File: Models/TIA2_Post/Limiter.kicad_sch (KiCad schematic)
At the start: 18 parts, among them J1 Conn_01x02_Pin, J2 Conn_01x02_Pin, J3 Conn_01x02_Pin, J4 Conn_01x02_Pin, Q1 Q_PNP, Q2 Q_NPN

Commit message: Save progress
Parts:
- removed J3, J4: Conn_01x02_Pin, symbol Connector:Conn_01x02_Pin
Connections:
- net Output is gone; now on net PostVoltage: R14.1, R15.1
- net PostVoltage: now also R8.1
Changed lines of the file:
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@@
+	(wire
+		(pts
+			(xy 207.01 105.41) (xy 205.74 105.41)
+		)
+		(stroke
+			(width 0)
+			(type default)
+		)
+	)
+	(wire
+		(pts
+			(xy 213.36 115.57) (xy 213.36 121.92)
+		)
+		(stroke
+			(width 0)
+			(type default)
+		)
+	)
+	(wire
+		(pts
+			(xy 96.52 96.52) (xy 111.76 96.52)
+		)
+		(stroke
+			(width 0)
+			(type default)
+		)
+	)
+	(wire
+		(pts
+			(xy 205.74 115.57) (xy 213.36 115.57)
+		)
+		(stroke
+			(width 0)
+			(type default)
+		)
+	)
+	(wire
+		(pts
+			(xy 86.36 88.9) (xy 86.36 96.52)
+		)
+		(stroke
+			(width 0)
+			(type default)
+		)
+	)
+	(wire
+		(pts
+			(xy 40.64 96.52) (xy 45.72 96.52)
+		)
+		(stroke
+			(width 0)
+			(type default)
+		)
+	)
+	(wire
+		(pts
+			(xy 172.72 142.24) (xy 177.8 142.24)
+		)
+		(stroke
+			(width 0)
+			(type default)
+		)
+	)
+	(wire
+		(pts
+			(xy 190.5 83.82) (xy 190.5 96.52)
+		)
+		(stroke
+			(width 0)
+			(type default)
+		)
+	)
+	(wire
+		(pts
+			(xy 213.36 88.9) (xy 213.36 90.17)
+		)
+		(stroke
+			(width 0)
+			(type default)
+		)
+	)
+	(wire
+		(pts
+			(xy 190.5 50.8) (xy 190.5 58.42)
+		)
+		(stroke
+			(width 0)
+			(type default)
+		)
+	)
+	(wire
+		(pts
+			(xy 213.36 114.3) (xy 213.36 115.57)
+		)
+		(stroke
+			(width 0)
+			(type default)
+		)
+	)
 	(wire
 		(pts
@@
 	(wire
 		(pts
-			(xy 207.01 105.41) (xy 205.74 105.41)
-		)
-		(stroke
-			(width 0)
-			(type default)
-		)
-	)
-	(wire
-		(pts
-			(xy 213.36 115.57) (xy 213.36 121.92)
-		)
-		(stroke
-			(width 0)
-			(type default)
-		)
-	)
-	(wire
-		(pts
-			(xy 96.52 96.52) (xy 111.76 96.52)
-		)
-		(stroke
-			(width 0)
-			(type default)
-		)
-	)
-	(wire
-		(pts
-			(xy 205.74 115.57) (xy 213.36 115.57)
-		)
-		(stroke
-			(width 0)
-			(type default)
-		)
-	)
-	(wire
-		(pts
-			(xy 86.36 88.9) (xy 86.36 96.52)
-		)
-		(stroke
-			(width 0)
-			(type default)
-		)
-	)
-	(wire
-		(pts
-			(xy 71.12 50.8) (xy 76.2 50.8)
-		)
-		(stroke
-			(width 0)
-			(type default)
-		)
-	)
-	(wire
-		(pts
-			(xy 40.64 96.52) (xy 45.72 96.52)
-		)
-		(stroke
-			(width 0)
-			(type default)
-		)
-	)
-	(wire
-		(pts
-			(xy 172.72 142.24) (xy 177.8 142.24)
-		)
-		(stroke
-			(width 0)
-			(type default)
-		)
-	)
-	(wire
-		(pts
-			(xy 190.5 83.82) (xy 190.5 96.52)
-		)
-		(stroke
-			(width 0)
-			(type default)
-		)
-	)
-	(wire
-		(pts
-			(xy 213.36 88.9) (xy 213.36 90.17)
-		)
-		(stroke
-			(width 0)
-			(type default)
-		)
-	)
-	(wire
-		(pts
-			(xy 190.5 50.8) (xy 190.5 58.42)
-		)
-		(stroke
-			(width 0)
-			(type default)
-		)
-	)
-	(wire
-		(pts
-			(xy 213.36 114.3) (xy 213.36 115.57)
-		)
-		(stroke
-			(width 0)
-			(type default)
-		)
-	)
-	(wire
-		(pts
 			(xy 201.93 121.92) (xy 213.36 121.92)
 		)
@@
 	(wire
 		(pts
-			(xy 78.74 50.8) (xy 96.52 50.8)
-		)
-		(stroke
-			(width 0)
-			(type default)
-		)
-	)
-	(wire
-		(pts
 			(xy 213.36 90.17) (xy 213.36 96.52)
 		)
@@
 		(pts
 			(xy 177.8 96.52) (xy 190.5 96.52)
-		)
-		(stroke
-			(width 0)
-			(type default)
-		)
-	)
-	(wire
-		(pts
-			(xy 96.52 66.04) (xy 96.52 76.2)
 		)
 		(stroke
@@
 		)
 	)
-	(label "Output"
-		(at 165.1 50.8 180)
-		(effects
-			(font
-				(size 1.27 1.27)
-			)
-			(justify right bottom)
-		)
-	)
-	(label "Output"
-		(at 96.52 50.8 0)
-		(effects
-			(font
-				(size 1.27 1.27)
-			)
-			(justify left bottom)
-		)
-	)
-	(label "Output"
-		(at 96.52 66.04 0)
-		(effects
-			(font
-				(size 1.27 1.27)
-			)
-			(justify left bottom)
-		)
-	)
 	(label "Clamped_Output"
 		(at 119.38 96.52 0)
@@
 			)
 			(justify left bottom)
-		)
-	)
-	(label "Output"
-		(at 165.1 142.24 180)
-		(effects
-			(font
-				(size 1.27 1.27)
-			)
-			(justify right bottom)
 		)
 	)
@@
 	(hierarchical_label "PostVoltage"
 		(shape input)
-		(at 71.12 50.8 180)
+		(at 165.1 142.24 180)
 		(effects
 			(font
@@
 		(shape input)
 		(at 213.36 142.24 270)
+		(effects
+			(font
+				(size 1.27 1.27)
+			)
+			(justify right)
+		)
+	)
+	(hierarchical_label "PostVoltage"
+		(shape input)
+		(at 96.52 78.74 90)
+		(effects
+			(font
+				(size 1.27 1.27)
+			)
+			(justify left)
+		)
+	)
+	(hierarchical_label "PostVoltage"
+		(shape input)
+		(at 165.1 50.8 180)
 		(effects
 			(font
@@
 	)
 	(symbol
-		(lib_id "Connector:Conn_01x02_Pin")
-		(at 78.74 45.72 270)
-		(unit 1)
-		(exclude_from_sim no)
-		(in_bom yes)
-		(on_board yes)
-		(dnp no)
-		(fields_autoplaced yes)
-		(property "Reference" "J3"
-			(at 80.01 45.0849 90)
-			(effects
-				(font
-					(size 1.27 1.27)
-				)
-				(justify left)
-			)
-		)
-		(property "Value" "Conn_01x02_Pin"
-			(at 80.01 47.6249 90)
-			(effects
-				(font
-					(size 1.27 1.27)
-				)
-				(justify left)
-			)
-		)
-		(property "Footprint" ""
-			(at 78.74 45.72 0)
-			(effects
-				(font
-					(size 1.27 1.27)
-				)
-				(hide yes)
-			)
-		)
-		(property "Datasheet" "~"
-			(at 78.74 45.72 0)
-			(effects
-				(font
-					(size 1.27 1.27)
-				)
-				(hide yes)
-			)
-		)
-		(property "Description" "Generic connector, single row, 01x02, script generated"
-			(at 78.74 45.72 0)
-			(effects
-				(font
-					(size 1.27 1.27)
-				)
-				(hide yes)
-			)
-		)
-		(pin "2"
-		)
-		(pin "1"
-		)
-		(instances
-			(project ""
-				(path "/f19129fc-f916-4692-924c-ee308c6b3e1d/26fbd804-20d9-4790-8391-a3b14d5c1dc5"
-					(reference "J3")
-					(unit 1)
-				)
-			)
-		)
-	)
-	(symbol
 		(lib_id "power:GND")
 		(at 226.06 96.52 90)
@@
 					(unit 1)
 				)
-			)
-		)
-	)
-	(symbol
-		(lib_id "Connector:Conn_01x02_Pin")
-		(at 91.44 76.2 0)
-		(unit 1)
-		(exclude_from_sim no)
-		(in_bom yes)
-		(on_board yes)
-		(dnp no)
-		(fields_autoplaced yes)
-		(property "Reference" "J4"
-			(at 92.075 71.12 0)
-			(effects
-				(font
-					(size 1.27 1.27)
-				)
-			)
-		)
-		(property "Value" "Conn_01x02_Pin"
-			(at 92.075 73.66 0)
-			(effects
-				(font
-					(size 1.27 1.27)
-				)
-			)
-		)
-		(property "Footprint" ""
-			(at 91.44 76.2 0)
-			(effects
-				(font
-					(size 1.27 1.27)
-				)
-				(hide yes)
-			)
-		)
-		(property "Datasheet" "~"
-			(at 91.44 76.2 0)
-			(effects
-				(font
-					(size 1.27 1.27)
-				)
-				(hide yes)
-			)
-		)
-		(property "Description" "Generic connector, single row, 01x02, script generated"
-			(at 91.44 76.2 0)
-			(effects
-				(font
-					(size 1.27 1.27)
-				)
-				(hide yes)
-			)
-		)
-		(pin "1"
-		)
-		(pin "2"
-		)
-		(instances
-			(project ""
-				(path "/f19129fc-f916-4692-924c-ee308c6b3e1d/26fbd804-20d9-4790-8391-a3b14d5c1dc5"
-					(reference "J4")
-					(unit 1)
-				)

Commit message: Save progress
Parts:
- removed Q1: Q_PNP, ThreeTerminal:SOT-23, symbol Custom:Q_PNP
- removed Q2: Q_NPN, ThreeTerminal:SOT-23, symbol Custom:Q_NPN
- added Q1: Q_NPN_BEC, symbol Custom:Q_NPN_BEC
- added Q3: Q_PNP_BEC, symbol Custom:Q_PNP_BEC
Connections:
- net Clamped_Output: now also Q1.3 (C), Q3.3 (C)
- net at D6.1 (K), R16.2: now also Q3.1 (B)
- net at D7.2 (A), D7.3 (*), R17.1: now also Q1.1 (B)
- net at D4.1 (K): now also Q3.2 (E)
- net at D5.2 (A): now also Q1.2 (E)
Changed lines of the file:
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@@
+	)
+	(symbol
+		(lib_id "Custom:Q_NPN_BEC")
+		(at 193.04 121.92 0)
+		(mirror y)
+		(unit 1)
+		(exclude_from_sim no)
+		(in_bom yes)
+		(on_board yes)
+		(dnp no)
+		(property "Reference" "Q1"
+			(at 185.42 123.1901 0)
+			(effects
+				(font
+					(size 1.27 1.27)
+				)
+				(justify left)
+			)
+		)
+		(property "Value" "Q_NPN_BEC"
+			(at 185.42 120.6501 0)
+			(effects
+				(font
+					(size 1.27 1.27)
+				)
+				(justify left)
+			)
+		)
+		(property "Footprint" ""
+			(at 193.04 121.92 0)
+			(effects
+				(font
+					(size 1.27 1.27)
+				)
+				(hide yes)
+			)
+		)
+		(property "Datasheet" ""
+			(at 193.04 121.92 0)
+			(effects
+				(font
+					(size 1.27 1.27)
+				)
+				(hide yes)
+			)
+		)
+		(property "Description" ""
+			(at 193.04 121.92 0)
+			(effects
+				(font
+					(size 1.27 1.27)
+				)
+				(hide yes)
+			)
+		)
+		(property "Purchase Link" "https://www.digikey.com/en/products/detail/onsemi/MMBT2222ALT1G/919593"
+			(at 193.04 121.92 0)
+			(effects
+				(font
+					(size 1.27 1.27)
+				)
+				(hide yes)
+			)
+		)
+		(pin "1"
+		)
+		(pin "3"
+		)
+		(pin "2"
+		)
+		(instances
+			(project ""
+				(path "/f19129fc-f916-4692-924c-ee308c6b3e1d/26fbd804-20d9-4790-8391-a3b14d5c1dc5"
+					(reference "Q1")
+					(unit 1)
+				)
+			)
+		)
 	)
 	(symbol
@@
 	)
 	(symbol
-		(lib_id "Custom:Q_PNP")
-		(at 193.04 71.12 180)
-		(unit 1)
-		(exclude_from_sim no)
-		(in_bom yes)
-		(on_board yes)
-		(dnp no)
-		(property "Reference" "Q1"
-			(at 185.42 72.3901 0)
-			(effects
-				(font
-					(size 1.27 1.27)
-				)
-				(justify left)
-			)
-		)
-		(property "Value" "Q_PNP"
-			(at 185.42 69.8501 0)
-			(effects
-				(font
-					(size 1.27 1.27)
-				)
-				(justify left)
-			)
-		)
-		(property "Footprint" "ThreeTerminal:SOT-23"
-			(at 193.04 71.12 0)
-			(effects
-				(font
-					(size 1.27 1.27)
-				)
-				(hide yes)
-			)
-		)
-		(property "Datasheet" ""
-			(at 193.04 71.12 0)
-			(effects
-				(font
-					(size 1.27 1.27)
-				)
-				(hide yes)
-			)
-		)
-		(property "Description" ""
-			(at 193.04 71.12 0)
-			(effects
-				(font
-					(size 1.27 1.27)
-				)
-				(hide yes)
-			)
-		)
-		(property "Purchase Link" "https://www.digikey.com/en/products/detail/onsemi/MMBT2907ALT1G/919599"
-			(at 193.04 71.12 0)
-			(effects
-				(font
-					(size 1.27 1.27)
-				)
-				(hide yes)
-			)
-		)
-		(property "Cost" ""
-			(at 193.04 71.12 0)
-			(effects
-				(font
-					(size 1.27 1.27)
-				)
-				(hide yes)
-			)
-		)
-		(property "RoHS Compliant" ""
-			(at 193.04 71.12 0)
-			(effects
-				(font
-					(size 1.27 1.27)
-				)
-				(hide yes)
-			)
-		)
-		(property "Cost (qty10)" ""
-			(at 193.04 71.12 0)
-			(effects
-				(font
-					(size 1.27 1.27)
-				)
-				(hide yes)
-			)
-		)
-		(pin "1"
-		)
-		(pin "3"
-		)
-		(pin "2"
-		)
-		(instances
-			(project "TIA2_Post"
-				(path "/f19129fc-f916-4692-924c-ee308c6b3e1d/26fbd804-20d9-4790-8391-a3b14d5c1dc5"
-					(reference "Q1")
-					(unit 1)
-				)
-			)
-		)
-	)
-	(symbol
-		(lib_id "Custom:Q_NPN")
-		(at 193.04 121.92 0)
-		(mirror y)
-		(unit 1)
-		(exclude_from_sim no)
-		(in_bom yes)
-		(on_board yes)
-		(dnp no)
-		(property "Reference" "Q2"
-			(at 185.42 120.6499 0)
-			(effects
-				(font
-					(size 1.27 1.27)
-				)
-				(justify left)
-			)
-		)
-		(property "Value" "Q_NPN"
-			(at 185.42 123.1899 0)
-			(effects
-				(font
-					(size 1.27 1.27)
-				)
-				(justify left)
-			)
-		)
-		(property "Footprint" "ThreeTerminal:SOT-23"
-			(at 193.04 121.92 0)
-			(effects
-				(font
-					(size 1.27 1.27)
-				)
-				(hide yes)
-			)
-		)
-		(property "Datasheet" ""
-			(at 193.04 121.92 0)
-			(effects
-				(font
-					(size 1.27 1.27)
-				)
-				(hide yes)
-			)
-		)
-		(property "Description" ""
-			(at 193.04 121.92 0)
-			(effects
-				(font
-					(size 1.27 1.27)
-				)
-				(hide yes)
-			)
-		)
-		(property "Purchase Link" "https://www.digikey.com/en/products/detail/onsemi/MMBT2222ALT1G/919593"
-			(at 193.04 121.92 0)
-			(effects
-				(font
-					(size 1.27 1.27)
-				)
-				(hide yes)
-			)
-		)
-		(property "Cost" ""
-			(at 193.04 121.92 0)
-			(effects
-				(font
-					(size 1.27 1.27)
-				)
-				(hide yes)
-			)
-		)
-		(property "RoHS Compliant" ""
-			(at 193.04 121.92 0)
-			(effects
-				(font
-					(size 1.27 1.27)
-				)
-				(hide yes)
-			)
-		)
-		(property "Cost (qty10)" ""
-			(at 193.04 121.92 0)
-			(effects
-				(font
-					(size 1.27 1.27)
-				)
-				(hide yes)
-			)
-		)
-		(pin "1"
-		)
-		(pin "3"
-		)
-		(pin "2"
-		)
-		(instances
-			(project "TIA2_Post"
-				(path "/f19129fc-f916-4692-924c-ee308c6b3e1d/26fbd804-20d9-4790-8391-a3b14d5c1dc5"
-					(reference "Q2")
-					(unit 1)
-				)
-			)
-		)
-	)
-	(symbol
 		(lib_id "Connector:Conn_01x02_Pin")
 		(at 48.26 91.44 270)
@@
 					(unit 1)
 				)
+			)
+		)
+	)
+	(symbol
+		(lib_id "Custom:Q_PNP_BEC")
+		(at 193.04 71.12 180)
+		(unit 1)
+		(exclude_from_sim no)
+		(in_bom yes)
+		(on_board yes)
+		(dnp no)
+		(fields_autoplaced yes)
+		(property "Reference" "Q3"
+			(at 185.42 69.8499 0)
+			(effects
+				(font
+					(size 1.27 1.27)
+				)
+				(justify left)
+			)
+		)
+		(property "Value" "Q_PNP_BEC"
+			(at 185.42 72.3899 0)
+			(effects
+				(font
+					(size 1.27 1.27)
+				)
+				(justify left)
+			)
+		)
+		(property "Footprint" ""
+			(at 193.04 71.12 0)
+			(effects
+				(font
+					(size 1.27 1.27)
+				)
+				(hide yes)
+			)
+		)
+		(property "Datasheet" ""
+			(at 193.04 71.12 0)
+			(effects
+				(font
+					(size 1.27 1.27)
+				)
+				(hide yes)
+			)
+		)
+		(property "Description" ""
+			(at 193.04 71.12 0)
+			(effects
+				(font
+					(size 1.27 1.27)
+				)
+				(hide yes)
+			)
+		)
+		(property "Purchase Link" "https://www.digikey.com/en/products/detail/onsemi/MMBT2907ALT1G/919599"
+			(at 193.04 71.12 0)
+			(effects
+				(font
+					(size 1.27 1.27)
+				)
+				(hide yes)
+			)
+		)
+		(pin "1"
+		)
+		(pin "3"
+		)
+		(pin "2"
+		)
+		(instances
+			(project ""
+				(path "/f19129fc-f916-4692-924c-ee308c6b3e1d/26fbd804-20d9-4790-8391-a3b14d5c1dc5"
+					(reference "Q3")
+					(unit 1)
+				)

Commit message: Save progress
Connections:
- net GND: no longer R7.2
- new net ISO_GND: R7.2
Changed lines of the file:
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@@
+		)
+	)
+	(global_label "ISO_GND"
+		(shape bidirectional)
+		(at 96.52 114.3 270)
+		(fields_autoplaced yes)
+		(effects
+			(font
+				(size 1.27 1.27)
+			)
+			(justify right)
+		)
+		(property "Intersheetrefs" "${INTERSHEET_REFS}"
+			(at 96.52 126.3794 90)
+			(effects
+				(font
+					(size 1.27 1.27)
+				)
+				(justify right)
+				(hide yes)
+			)
+		)
+	)
+	(global_label "-15V"
+		(shape input)
+		(at 213.36 142.24 270)
+		(fields_autoplaced yes)
+		(effects
+			(font
+				(size 1.27 1.27)
+			)
+			(justify right)
+		)
+		(property "Intersheetrefs" "${INTERSHEET_REFS}"
+			(at 213.36 150.3052 90)
+			(effects
+				(font
+					(size 1.27 1.27)
+				)
+				(justify right)
+				(hide yes)
+			)
+		)
+	)
+	(global_label "15V"
+		(shape input)
+		(at 213.36 48.26 90)
+		(fields_autoplaced yes)
+		(effects
+			(font
+				(size 1.27 1.27)
+			)
+			(justify left)
+		)
+		(property "Intersheetrefs" "${INTERSHEET_REFS}"
+			(at 213.36 41.7672 90)
+			(effects
+				(font
+					(size 1.27 1.27)
+				)
+				(justify left)
+				(hide yes)
+			)
 		)
 	)
@@
 		(shape input)
 		(at 165.1 142.24 180)
-		(effects
-			(font
-				(size 1.27 1.27)
-			)
-			(justify right)
-		)
-	)
-	(hierarchical_label "15V"
-		(shape input)
-		(at 213.36 48.26 90)
-		(effects
-			(font
-				(size 1.27 1.27)
-			)
-			(justify left)
-		)
-	)
-	(hierarchical_label "-15V"
-		(shape input)
-		(at 213.36 142.24 270)
 		(effects
 			(font
@@
 					(unit 1)
 				)
-			)
-		)
-	)
-	(symbol
-		(lib_id "power:GND")
-		(at 96.52 114.3 0)
-		(unit 1)
-		(exclude_from_sim no)
-		(in_bom yes)
-		(on_board yes)
-		(dnp no)
-		(fields_autoplaced yes)
-		(property "Reference" "#PWR05"
-			(at 96.52 120.65 0)
-			(effects
-				(font
-					(size 1.27 1.27)
-				)
-				(hide yes)
-			)
-		)
-		(property "Value" "GND"
-			(at 96.52 119.38 0)
-			(effects
-				(font
-					(size 1.27 1.27)
-				)
-			)
-		)
-		(property "Footprint" ""
-			(at 96.52 114.3 0)
-			(effects
-				(font
-					(size 1.27 1.27)
-				)
-				(hide yes)
-			)
-		)
-		(property "Datasheet" ""
-			(at 96.52 114.3 0)
-			(effects
-				(font
-					(size 1.27 1.27)
-				)
-				(hide yes)
-			)
-		)
-		(property "Description" "Power symbol creates a global label with name \"GND\" , ground"
-			(at 96.52 114.3 0)
-			(effects
-				(font
-					(size 1.27 1.27)
-				)
-				(hide yes)
-			)
-		)
-		(pin "1"
-		)
-		(instances
-			(project ""
-				(path "/f19129fc-f916-4692-924c-ee308c6b3e1d/26fbd804-20d9-4790-8391-a3b14d5c1dc5"
-					(reference "#PWR05")
-					(unit 1)
-				)

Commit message: Save progress
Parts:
- R8: value 150k, 1% -> 240k, 1%; Purchase Link https://www.digikey.com/en/products/detail/vishay-dale/CRCW0603150KFKEA/1174914 -> https://www.digikey.com/en/products/detail/vishay-dale/CRCW0603240KFKEA/1174937
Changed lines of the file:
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@@
-			)
-		)
-		(property "RoHS Compliant" ""
-			(at 96.52 105.41 0)
-			(effects
-				(font
-					(size 1.27 1.27)
-				)
-				(hide yes)
-			)
-		)
-		(property "Cost (qty10)" ""
-			(at 96.52 105.41 0)
-			(effects
-				(font
-					(size 1.27 1.27)
-				)
-				(hide yes)
 			)
 		)
@@
 			)
 		)
-		(property "Value" "150k, 1%"
+		(property "Value" "240k, 1%"
 			(at 99.06 88.8999 0)
 			(effects
@@
 			)
 		)
-		(property "Purchase Link" "https://www.digikey.com/en/products/detail/vishay-dale/CRCW0603150KFKEA/1174914"
+		(property "Purchase Link" "https://www.digikey.com/en/products/detail/vishay-dale/CRCW0603240KFKEA/1174937"
 			(at 96.52 87.63 0)
 			(effects

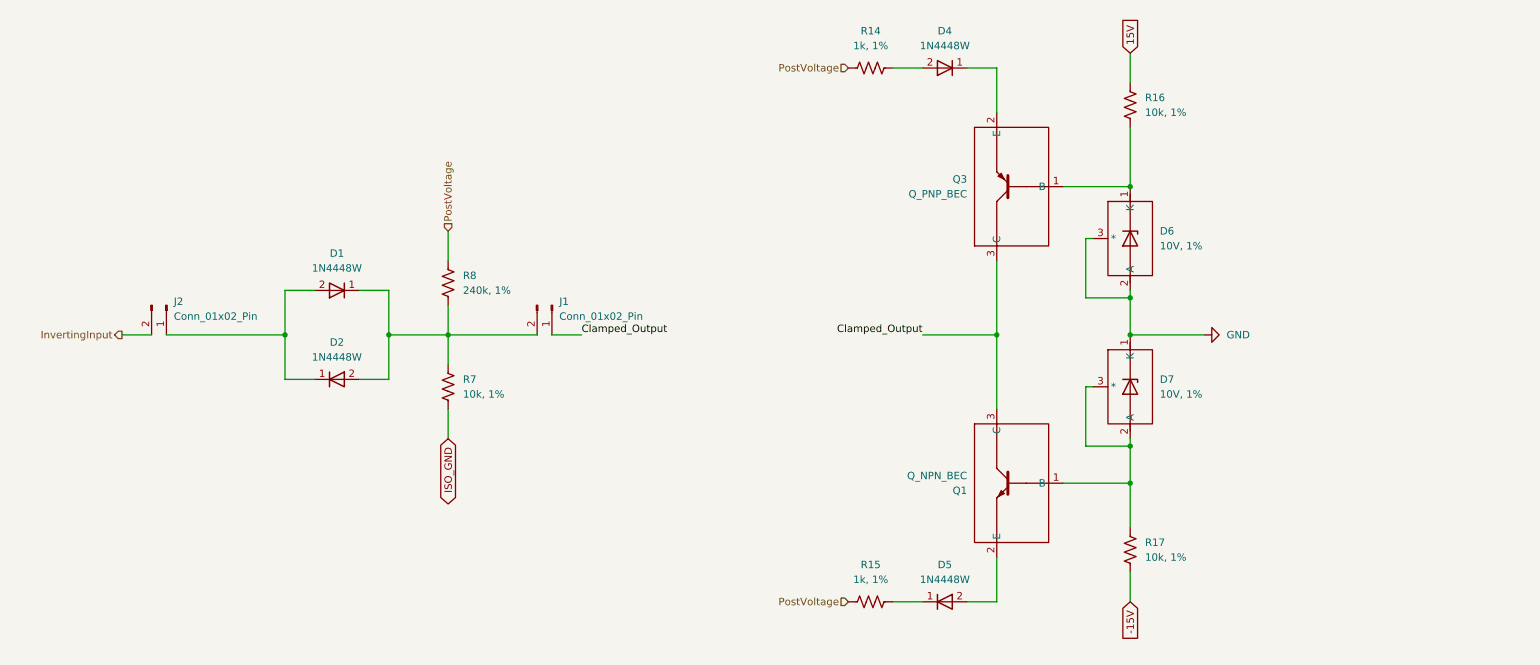
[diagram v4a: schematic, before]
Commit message: ERC passes for the two new boards
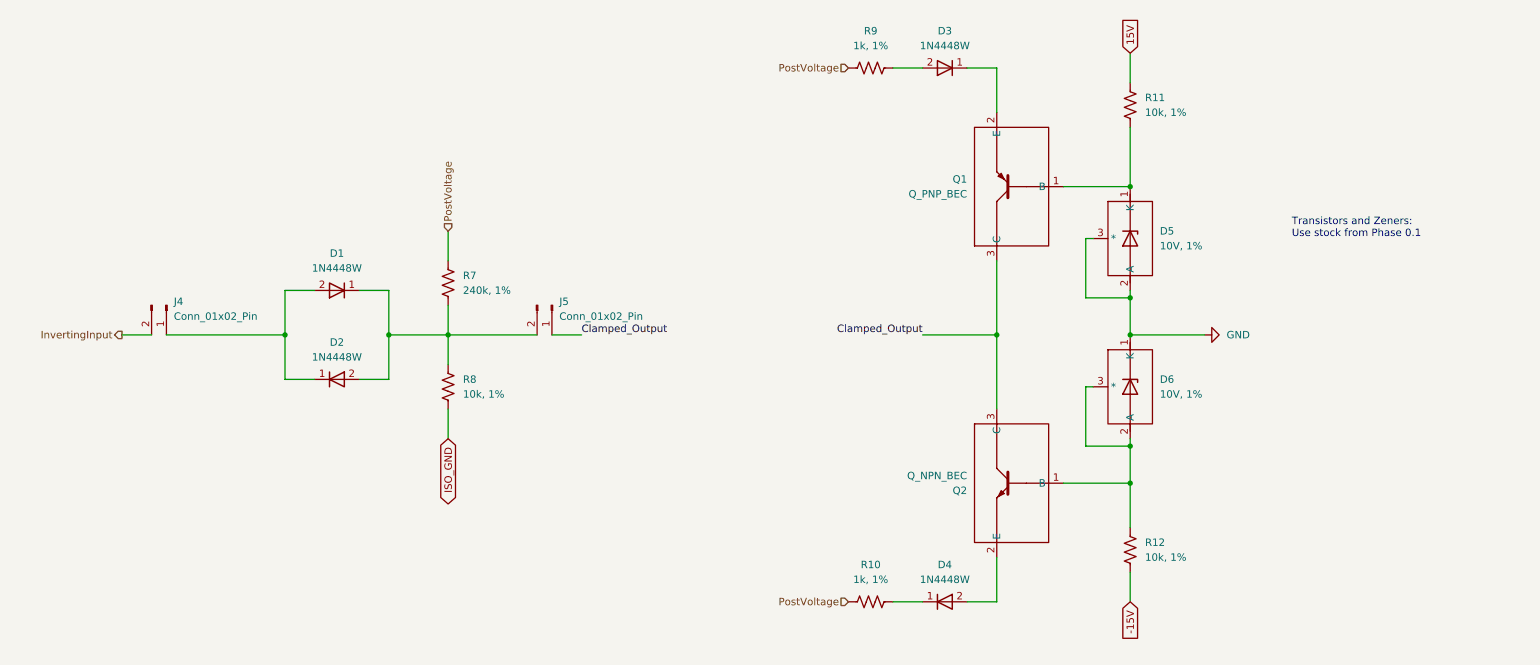
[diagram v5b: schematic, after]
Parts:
- D1, D2: Cost (none) -> $0.146
- D3: renamed from D4; Cost (none) -> $0.146
- D4: renamed from D5; Cost (none) -> $0.146
- D5: renamed from D6; Purchase Link https://www.digikey.com/en/products/detail/texas-instrument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 -> (none); now left out of the parts list
- D6: renamed from D7; Purchase Link https://www.digikey.com/en/products/detail/texas-instrument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 -> (none); now left out of the parts list
- J4: renamed from J2; footprint (none) -> Connector_Custom:PinHeader_1x2; Cost (none) -> $0.563; Purchase Link (none) -> https://www.digikey.com/en/products/detail/sullins-connecto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
- J5: renamed from J1; footprint (none) -> Connector_Custom:PinHeader_1x2; Cost (none) -> $0.563; Purchase Link (none) -> https://www.digikey.com/en/products/detail/sullins-connecto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
- Q1: renamed from Q3; footprint (none) -> ThreeTerminal:SOT-23; Purchase Link https://www.digikey.com/en/products/detail/onsemi/MMBT2907A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 -> (none); now left out of the parts list
- Q2: renamed from Q1; footprint (none) -> ThreeTerminal:SOT-23; Purchase Link https://www.digikey.com/en/products/detail/onsemi/MMBT2222A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 -> (none); now left out of the parts list
- R10: renamed from R15; Cost (none) -> $0.030
- R11: renamed from R16; Cost (none) -> $0.030
- R12: renamed from R17; Cost (none) -> $0.030
- R7: renamed from R8; Cost (none) -> $0.030
- R8: renamed from R7; Cost (none) -> $0.030
- R9: renamed from R14; Cost (none) -> $0.030
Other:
- note added: "Transistors and Zeners: Use stock from Phase 0.1"
